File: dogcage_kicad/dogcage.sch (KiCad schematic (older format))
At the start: 18 parts, among them CON1 BARREL_JACK, M1 XBEE, P1 Door Sensor, P2 Servo, P3 CONN_01X10, P4 CONN_01X10, P5 CONN_01X14, P6 CONN_01X05, P7 CONN_01X14, Q1 TIP120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

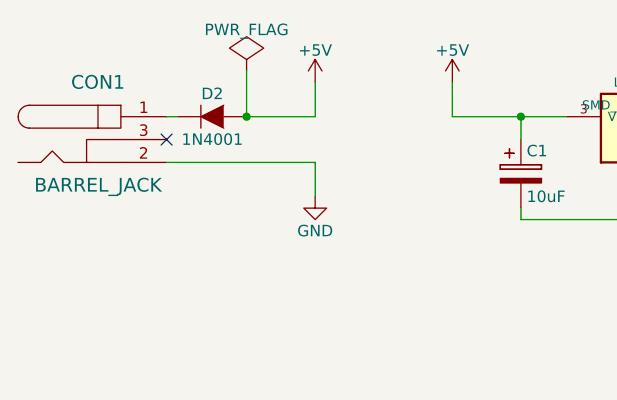
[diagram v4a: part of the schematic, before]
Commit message: Fixed diode orientation and layout WIP
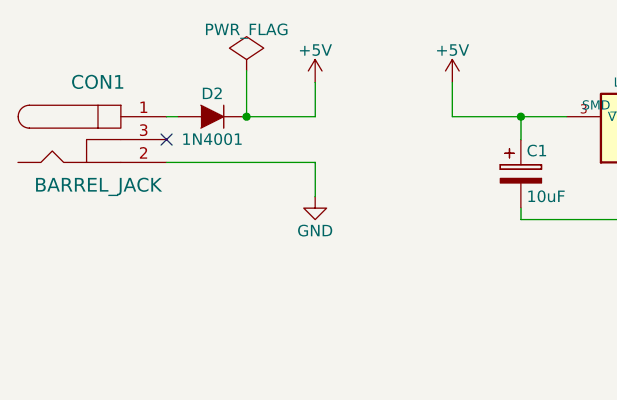
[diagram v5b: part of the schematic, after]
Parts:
- C1: footprint (none) -> Capacitors_Elko_ThroughHole:Elko_vert_11x5mm_RM2
- C2: footprint (none) -> Capacitors_Elko_ThroughHole:Elko_vert_20x10mm_RM5
- D1: footprint (none) -> LEDs:LED-3MM
- D2: footprint (none) -> Diodes_ThroughHole:Diode_DO-41_SOD81_Horizontal_RM10
- M1: footprint xbee_r1-XBEE -> modules:xbee
- P3, P4: footprint (none) -> Pin_Headers:Pin_Header_Straight_1x10
- P5, P7: footprint (none) -> Pin_Headers:Pin_Header_Straight_1x14
- P6: footprint (none) -> Pin_Headers:Pin_Header_Straight_1x05
- R1: footprint (none) -> Resistors_ThroughHole:Resistor_Horizontal_RM20mm
- U2: footprint MODULE -> modules:Teensy-3.1
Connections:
- net +5V: now also D2.1 (K); no longer D2.2 (A)
- net at CON1.1: now also D2.2 (A); no longer D2.1 (K)
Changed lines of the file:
@@
 LIBS:memory
 LIBS:xilinx
-LIBS:special
 LIBS:microcontrollers
 LIBS:dsp
@@
 F 0 "U2" H 7650 1850 50  0000 C CNN
 F 1 "TEENSYLC" H 7650 2050 50  0000 C CNN
-F 2 "MODULE" H 7650 1950 50  0001 C CNN
+F 2 "modules:Teensy-3.1" H 7650 1950 50  0001 C CNN
 F 3 "DOCUMENTATION" H 7650 1950 50  0001 C CNN
 	1    7650 1950
@@
 F 0 "C1" H 3275 1500 50  0000 L CNN
 F 1 "10uF" H 3275 1300 50  0000 L CNN
-F 2 "" H 3288 1250 30  0001 C CNN
+F 2 "Capacitors_Elko_ThroughHole:Elko_vert_11x5mm_RM2" H 3288 1250 30  0001 C CNN
 F 3 "" H 3250 1400 60  0000 C CNN
 	1    3250 1400
@@
 F 0 "C2" H 4475 1500 50  0000 L CNN
 F 1 "10uF" H 4475 1300 50  0000 L CNN
-F 2 "" H 4488 1250 30  0001 C CNN
+F 2 "Capacitors_Elko_ThroughHole:Elko_vert_20x10mm_RM5" H 4488 1250 30  0001 C CNN
 F 3 "" H 4450 1400 60  0000 C CNN
 	1    4450 1400
@@
 F 0 "D1" H 4000 4750 50  0000 C CNN
 F 1 "Assoc LED" H 4000 4550 50  0000 C CNN
-F 2 "" H 4000 4650 60  0000 C CNN
+F 2 "LEDs:LED-3MM" H 4000 4650 60  0001 C CNN
 F 3 "" H 4000 4650 60  0000 C CNN
 	1    4000 4650
@@
 F 0 "R1" V 4080 4200 50  0000 C CNN
 F 1 "330" V 4000 4200 50  0000 C CNN
-F 2 "" V 3930 4200 30  0000 C CNN
+F 2 "Resistors_ThroughHole:Resistor_Horizontal_RM20mm" V 3930 4200 30  0001 C CNN
 F 3 "" H 4000 4200 30  0000 C CNN
 	1    4000 4200
@@
 F 0 "D2" H 1900 1250 50  0000 C CNN
 F 1 "1N4001" H 1900 1050 50  0000 C CNN
-F 2 "" H 1900 1150 60  0000 C CNN
+F 2 "Diodes_ThroughHole:Diode_DO-41_SOD81_Horizontal_RM10" H 1900 1150 60  0001 C CNN
 F 3 "" H 1900 1150 60  0000 C CNN
 	1    1900 1150
-	1    0    0    -1
+	-1   0    0    -1
 $EndComp
 Wire Wire Line
@@
 F 0 "M1" H 2150 4550 50  0000 L BNN
 F 1 "XBEE" H 2100 3050 50  0000 L BNN
-F 2 "xbee_r1-XBEE" H 2850 3700 50  0001 C CNN
+F 2 "modules:xbee" H 2850 3700 50  0001 C CNN
 F 3 "" H 2850 3550 60  0000 C CNN
 	1    2850 3550
@@
 F 0 "P3" H 1300 3950 50  0000 C CNN
 F 1 "CONN_01X10" V 1400 3400 50  0000 C CNN
-F 2 "" H 1300 3400 60  0000 C CNN
+F 2 "Pin_Headers:Pin_Header_Straight_1x10" H 1300 3400 60  0001 C CNN
 F 3 "" H 1300 3400 60  0000 C CNN
 	1    1300 3400
@@
 F 0 "P4" H 4500 3950 50  0000 C CNN
 F 1 "CONN_01X10" V 4600 3400 50  0000 C CNN
-F 2 "" H 4500 3400 60  0000 C CNN
+F 2 "Pin_Headers:Pin_Header_Straight_1x10" H 4500 3400 60  0001 C CNN
 F 3 "" H 4500 3400 60  0000 C CNN
 	1    4500 3400
@@
 F 0 "P7" H 9300 2700 50  0000 C CNN
 F 1 "CONN_01X14" V 9400 1950 50  0000 C CNN
-F 2 "" H 9300 1950 60  0000 C CNN
+F 2 "Pin_Headers:Pin_Header_Straight_1x14" H 9300 1950 60  0001 C CNN
 F 3 "" H 9300 1950 60  0000 C CNN
 	1    9300 1950
@@
 F 0 "P5" H 5850 2700 50  0000 C CNN
 F 1 "CONN_01X14" V 5950 1950 50  0000 C CNN
-F 2 "" H 5850 1950 60  0000 C CNN
+F 2 "Pin_Headers:Pin_Header_Straight_1x14" H 5850 1950 60  0001 C CNN
 F 3 "" H 5850 1950 60  0000 C CNN
 	1    5850 1950
@@
 F 0 "P6" H 7650 3700 50  0000 C CNN
 F 1 "CONN_01X05" V 7750 3400 50  0000 C CNN
-F 2 "" H 7650 3400 60  0000 C CNN
+F 2 "Pin_Headers:Pin_Header_Straight_1x05" H 7650 3400 60  0001 C CNN
 F 3 "" H 7650 3400 60  0000 C CNN
 	1    7650 3400

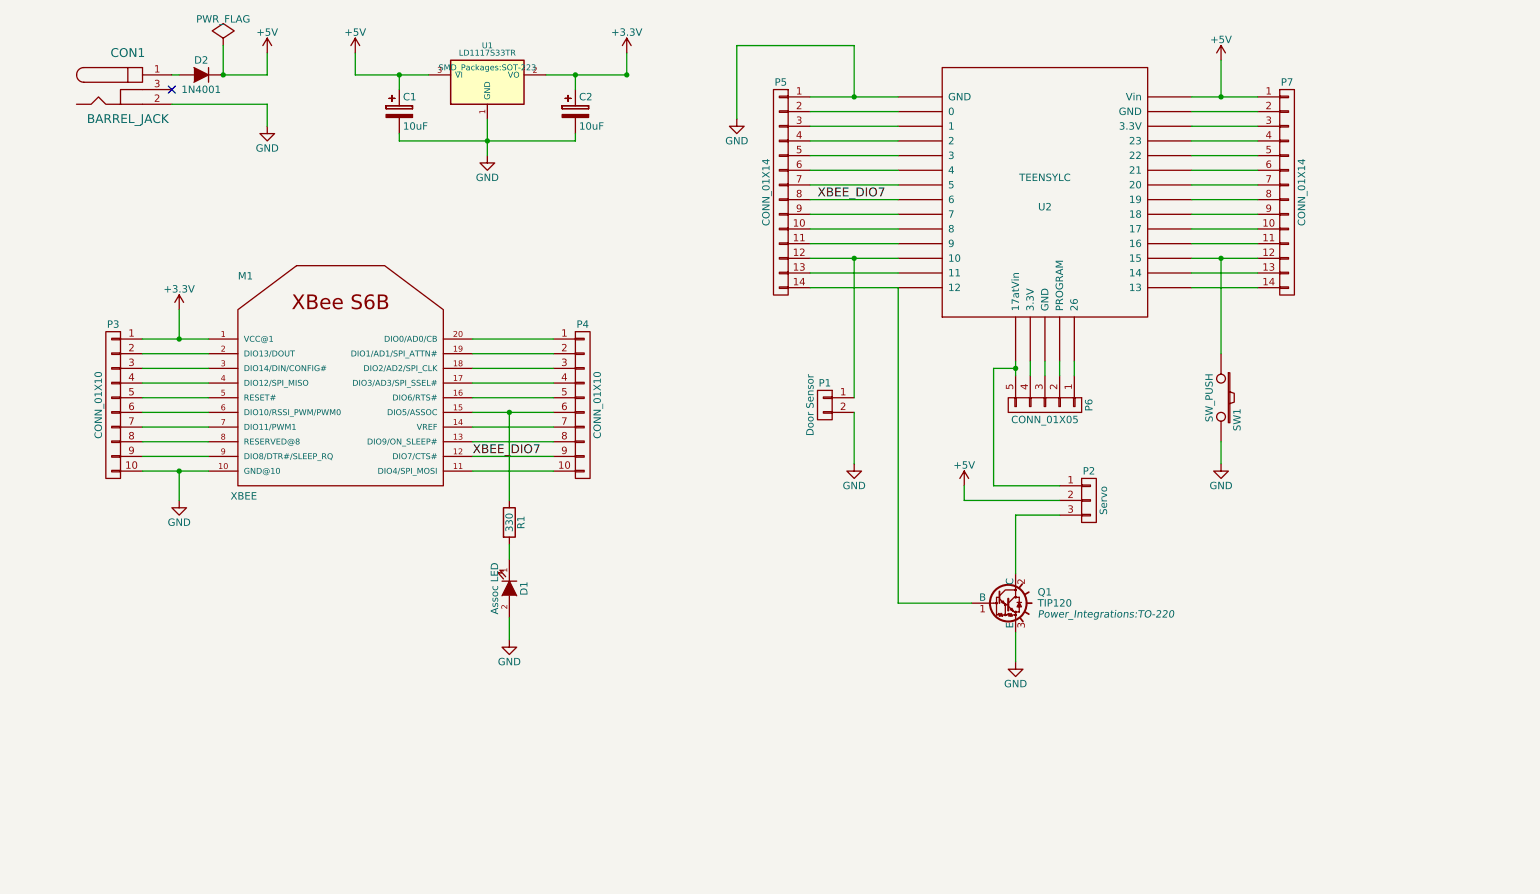
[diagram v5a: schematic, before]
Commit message: Fixed orientation of LED
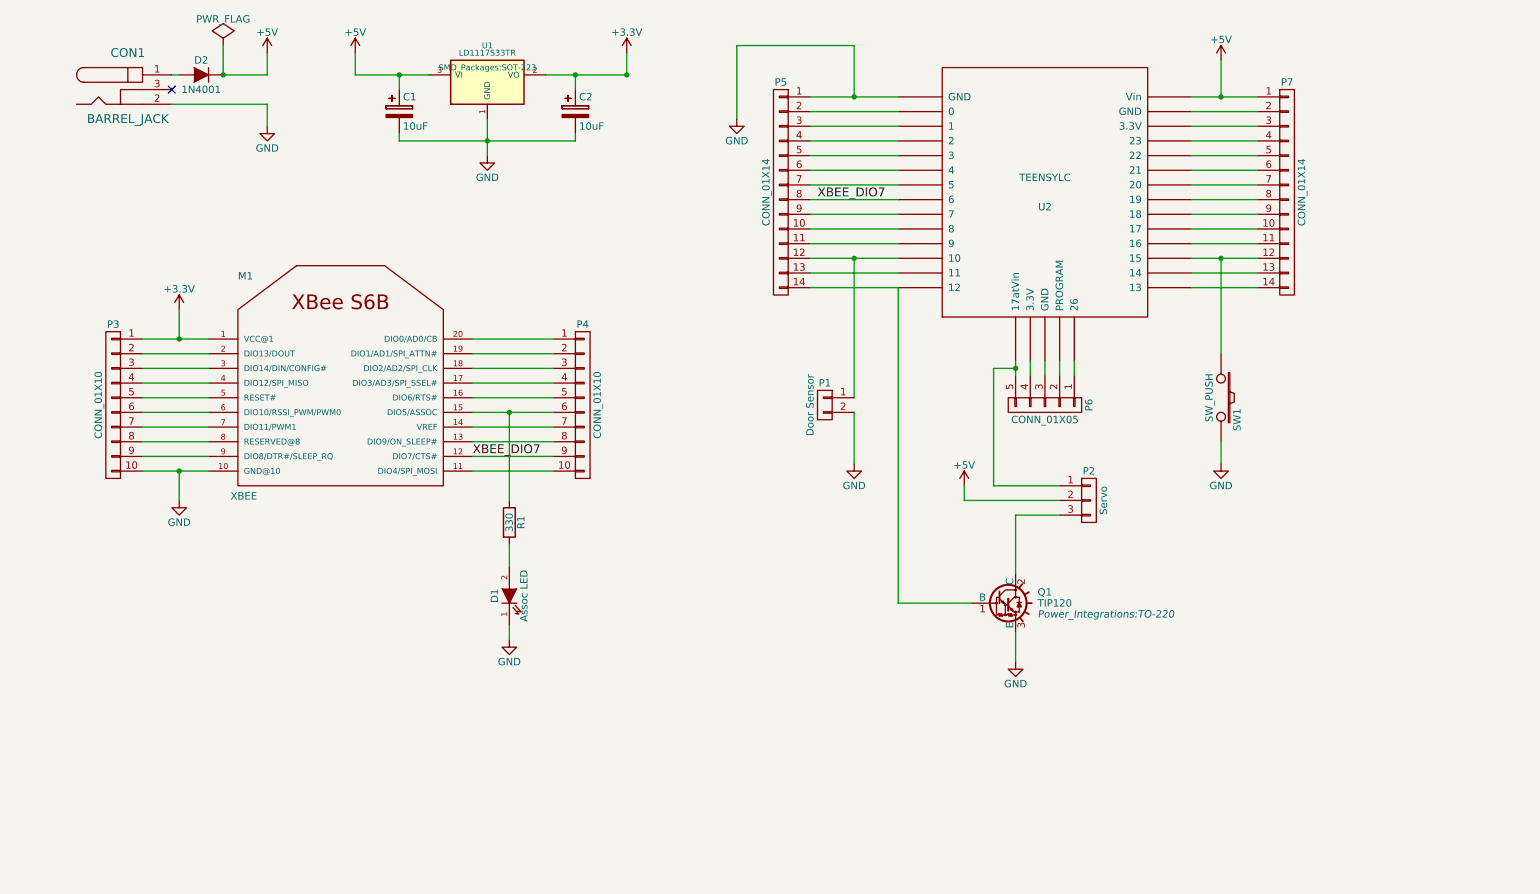
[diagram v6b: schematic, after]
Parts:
- C2: footprint Capacitors_Elko_ThroughHole:Elko_vert_20x10mm_RM5 -> Capacitors_Elko_ThroughHole:Elko_vert_11x5mm_RM2
- R1: footprint Resistors_ThroughHole:Resistor_Horizontal_RM20mm -> Resistors_ThroughHole:Resistor_Horizontal_RM10mm
- SW1: footprint Buttons_Switches_ThroughHole:SW_PUSH -> Buttons_Switches_ThroughHole:SW_PUSH_SMALL
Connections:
- net GND: now also D1.1 (K); no longer D1.2 (A)
- net at R1.2: now also D1.2 (A); no longer D1.1 (K)
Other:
- moved on the sheet: D1
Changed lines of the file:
@@
-$EndComp
-$Comp
-L SW_PUSH SW1
-U 1 1 553C46F2
-P 8850 3350
-F 0 "SW1" H 9000 3460 50  0000 C CNN
-F 1 "SW_PUSH" H 8850 3270 50  0000 C CNN
-F 2 "Buttons_Switches_ThroughHole:SW_PUSH" H 8850 3350 60  0001 C CNN
-F 3 "" H 8850 3350 60  0000 C CNN
-	1    8850 3350
-	0    1    1    0
 $EndComp
 $Comp
@@
 F 0 "C2" H 4475 1500 50  0000 L CNN
 F 1 "10uF" H 4475 1300 50  0000 L CNN
-F 2 "Capacitors_Elko_ThroughHole:Elko_vert_20x10mm_RM5" H 4488 1250 30  0001 C CNN
+F 2 "Capacitors_Elko_ThroughHole:Elko_vert_11x5mm_RM2" H 4488 1250 30  0001 C CNN
 F 3 "" H 4450 1400 60  0000 C CNN
 	1    4450 1400
@@
 L LED D1
 U 1 1 553D18EC
-P 4000 4650
-F 0 "D1" H 4000 4750 50  0000 C CNN
-F 1 "Assoc LED" H 4000 4550 50  0000 C CNN
-F 2 "LEDs:LED-3MM" H 4000 4650 60  0001 C CNN
-F 3 "" H 4000 4650 60  0000 C CNN
-	1    4000 4650
-	0    1    1    0
+P 4000 4700
+F 0 "D1" H 4000 4800 50  0000 C CNN
+F 1 "Assoc LED" H 4000 4600 50  0000 C CNN
+F 2 "LEDs:LED-3MM" H 4000 4700 60  0001 C CNN
+F 3 "" H 4000 4700 60  0000 C CNN
+	1    4000 4700
+	0    -1   -1   0
 $EndComp
 $Comp
@@
 F 0 "R1" V 4080 4200 50  0000 C CNN
 F 1 "330" V 4000 4200 50  0000 C CNN
-F 2 "Resistors_ThroughHole:Resistor_Horizontal_RM20mm" V 3930 4200 30  0001 C CNN
+F 2 "Resistors_ThroughHole:Resistor_Horizontal_RM10mm" V 3930 4200 30  0001 C CNN
 F 3 "" H 4000 4200 30  0000 C CNN
 	1    4000 4200
@@
 	7450 4150 7750 4150
 Wire Wire Line
-	4250 1150 4800 1150
+	4250 1150 4450 1150
+Wire Wire Line
+	4450 1150 4800 1150
 Wire Wire Line
 	4800 1150 4800 1000
 Wire Wire Line
-	3850 1450 3850 1700
+	3850 1450 3850 1600
+Wire Wire Line
+	3850 1600 3850 1700
 Wire Wire Line
 	3250 1550 3250 1600
 Wire Wire Line
-	3250 1600 4450 1600
+	3250 1600 3850 1600
+Wire Wire Line
+	3850 1600 4450 1600
 Connection ~ 3850 1600
 Wire Wire Line
@@
 	6350 3450 6350 3800
 Wire Wire Line
-	4000 5000 4000 4850
-Wire Wire Line
-	4000 4350 4000 4450
+	4000 5000 4000 4900
+Wire Wire Line
+	4000 4350 4000 4500
 Wire Wire Line
 	1700 1150 1750 1150
@@
 	2950 1000 2950 1150
 Wire Wire Line
-	2950 1150 3450 1150
+	2950 1150 3250 1150
+Wire Wire Line
+	3250 1150 3450 1150
 Wire Wire Line
 	3250 1250 3250 1150
@@
 $EndComp
 Wire Wire Line
-	1500 2950 1950 2950
+	1500 2950 1750 2950
+Wire Wire Line
+	1750 2950 1950 2950
 Wire Wire Line
 	1500 3050 1950 3050
@@
 $EndComp
 Wire Wire Line
-	3750 3450 4300 3450
+	3750 3450 4000 3450
+Wire Wire Line
+	4000 3450 4300 3450
 Wire Wire Line
 	4000 3450 4000 4050
@@
 	6350 2400 6350 3350
 Wire Wire Line
-	6050 2400 6650 2400
+	6050 2400 6350 2400
+Wire Wire Line
+	6350 2400 6650 2400
 Wire Wire Line
 	6650 2600 6050 2600
@@
 	6650 1400 6050 1400
 Wire Wire Line
-	8650 2400 9100 2400
+	8650 2400 8850 2400
+Wire Wire Line
+	8850 2400 9100 2400
 Wire Wire Line
 	8850 3050 8850 2400
@@
 	8650 1400 9100 1400
 Wire Wire Line
-	8650 1300 9100 1300
+	8650 1300 8850 1300
+Wire Wire Line
+	8850 1300 9100 1300
 Connection ~ 8850 1300
 Wire Wire Line
@@
 	6650 4750 7150 4750
 Wire Wire Line
-	7450 3100 7450 3200
+	7450 3100 7450 3150
+Wire Wire Line
+	7450 3150 7450 3200
 Wire Wire Line
 	7450 3150 7300 3150
@@
 	7850 3100 7850 3200
 Wire Wire Line
-	1500 3850 1950 3850
+	1500 3850 1750 3850
+Wire Wire Line
+	1750 3850 1950 3850
 Wire Wire Line
 	1750 3850 1750 4050
 Connection ~ 1750 3850
 Wire Wire Line
-	6050 1300 6650 1300
+	6050 1300 6350 1300
+Wire Wire Line
+	6350 1300 6650 1300
 Wire Wire Line
 	6350 1300 6350 950
@@
 Connection ~ 6350 1300
 Connection ~ 6350 2400
+$Comp
+L SW_PUSH SW1
+U 1 1 553C46F2
+P 8850 3350
+F 0 "SW1" H 9000 3460 50  0000 C CNN
+F 1 "SW_PUSH" H 8850 3270 50  0000 C CNN
+F 2 "Buttons_Switches_ThroughHole:SW_PUSH_SMALL" H 8850 3350 60  0001 C CNN
+F 3 "" H 8850 3350 60  0000 C CNN
+	1    8850 3350
+	0    1    1    0
+$EndComp
 $EndSCHEMATC

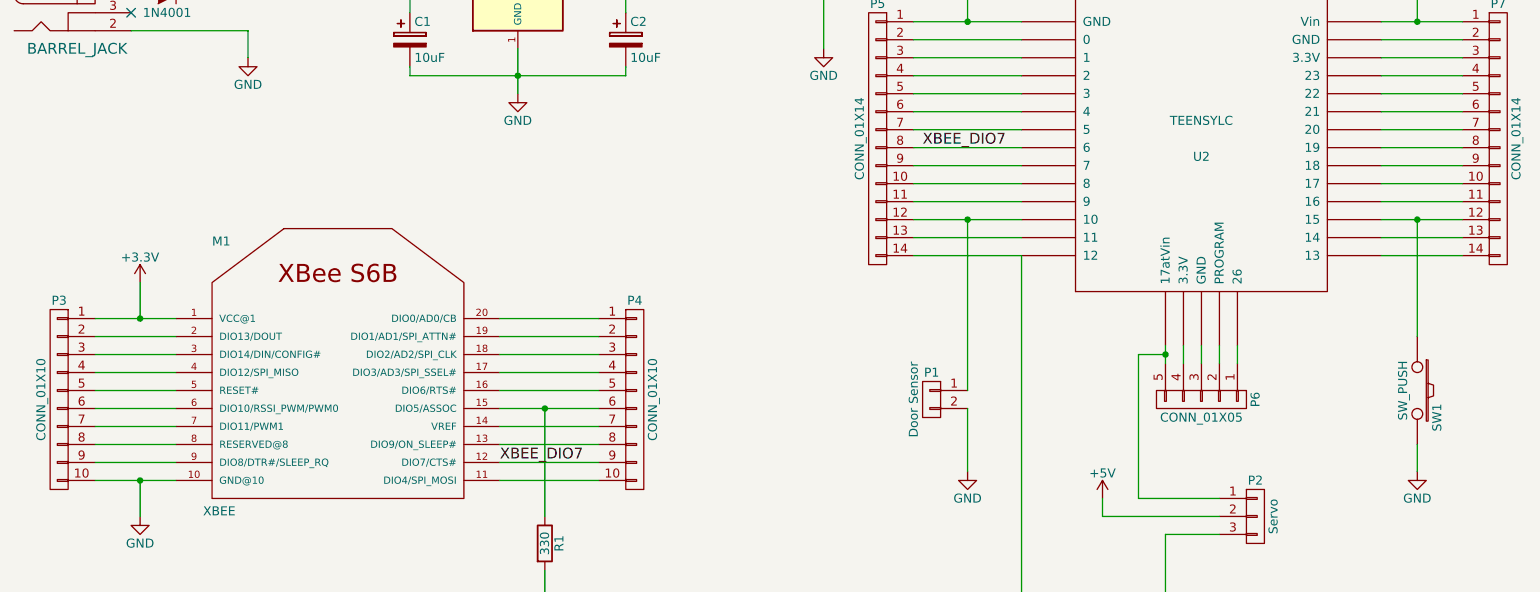
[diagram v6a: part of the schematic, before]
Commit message: Moved XBee control line to make layout easier
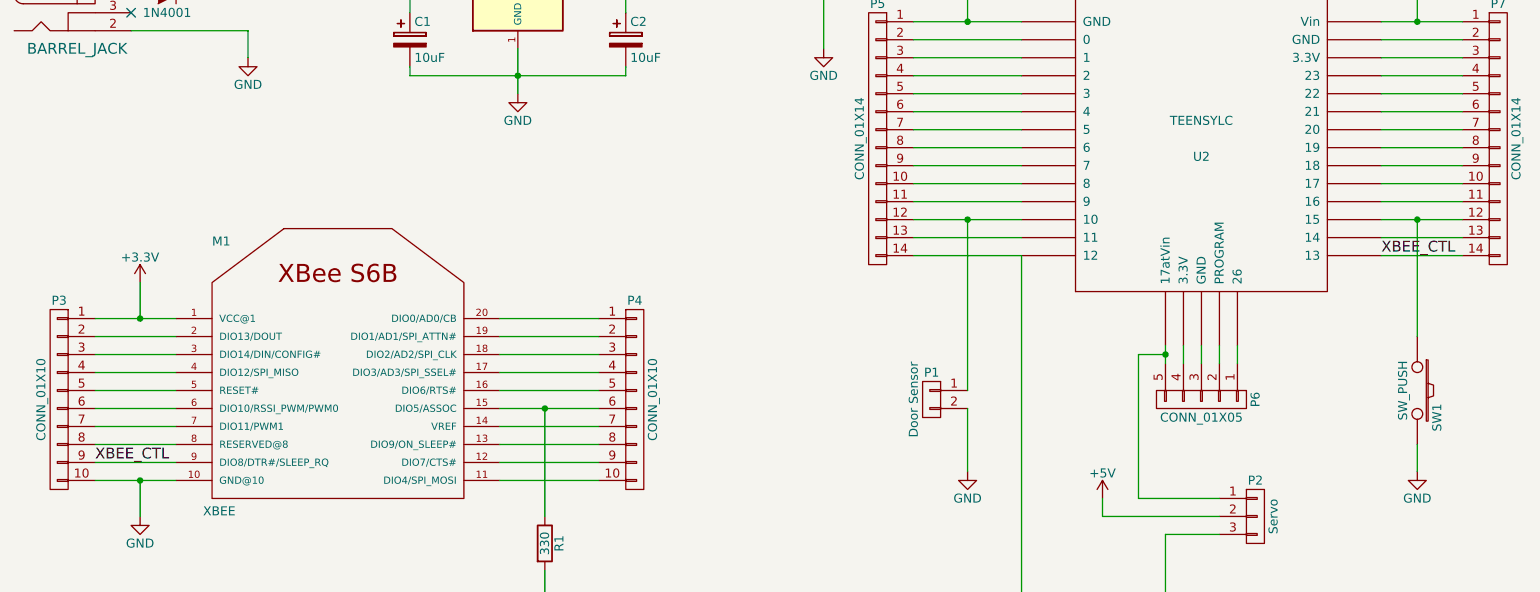
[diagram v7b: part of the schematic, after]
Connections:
- net XBEE_CTL: now reaches P7.14 (P14), U2.20 (13)
- net XBEE_CTL: now also M1.9 (DIO8/DTR#/SLEEP_RQ), P3.9 (P9)
- net XBEE_DIO7: no longer names the net of P5.8 (P8), U2.8 (6)
- net XBEE_DIO7: no longer M1.12 (DIO7/CTS#), P4.9 (P9)
- new net: M1.12 (DIO7/CTS#), P4.9 (P9)
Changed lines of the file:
@@
 	1750 2750 1750 2950
 Connection ~ 1750 2950
-Text Label 3750 3750 0    60   ~ 0
-XBEE_DIO7
 Wire Wire Line
 	6650 2000 6050 2000
-Text Label 6100 2000 0    60   ~ 0
-XBEE_DIO7
 $Comp
 L CONN_01X14 P7
@@
 	0    1    1    0
 $EndComp
+Text Label 8650 2600 0    60   ~ 0
+XBEE_CTL
+Text Label 1500 3750 0    60   ~ 0
+XBEE_CTL
 $EndSCHEMATC
